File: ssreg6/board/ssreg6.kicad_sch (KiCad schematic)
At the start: 74 parts, among them J12 PROG, U1 YS-12V450A, U2 LTV-354T, U3 ESP32-C3-WROOM-02, U3 FR8205, U5 LM358, U6 LM358, U7 LM358, X1 MAINS, X2 TARIFF

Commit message: WIP
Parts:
- removed H1 (x4): MountingHole, MountingHole:MountingHole_3.7mm_Pad_Via, symbol Mechanical:MountingHole
- removed U1: YS-12V450A, Drake:YS-12V450A, symbol Drake:PSU
- added J2: Display, Connector_PinHeader_2.54mm:PinHeader_1x03_P2.54mm_Vertical, symbol Connector_Generic:Conn_01x03
- added R10, R5, R6, R7, R8, R9: 100k, Resistor_SMD:R_0805_2012Metric_Pad1.20x1.40mm_HandSolder, symbol Device:R
- C10: renamed from C13; footprint Capacitor_SMD:C_0805_2012Metric -> Capacitor_SMD:C_0805_2012Metric_Pad1.18x1.45mm_HandSolder
- C11: renamed from C14; footprint Capacitor_SMD:C_0805_2012Metric -> Capacitor_SMD:C_0805_2012Metric_Pad1.18x1.45mm_HandSolder
- C12: renamed from C15; footprint Capacitor_SMD:C_0805_2012Metric -> Capacitor_SMD:C_0805_2012Metric_Pad1.18x1.45mm_HandSolder
- C13: renamed from C16; footprint Capacitor_SMD:C_0805_2012Metric -> Capacitor_SMD:C_0805_2012Metric_Pad1.18x1.45mm_HandSolder
- C14: renamed from C10; footprint Capacitor_SMD:C_0805_2012Metric -> Capacitor_SMD:C_0805_2012Metric_Pad1.18x1.45mm_HandSolder
- C15: renamed from C17; footprint Capacitor_SMD:C_0805_2012Metric -> Capacitor_SMD:C_0805_2012Metric_Pad1.18x1.45mm_HandSolder
- C16: renamed from C18; footprint Capacitor_SMD:C_0805_2012Metric -> Capacitor_SMD:C_0805_2012Metric_Pad1.18x1.45mm_HandSolder
- C17: renamed from C19; footprint Capacitor_SMD:C_0805_2012Metric -> Capacitor_SMD:C_0805_2012Metric_Pad1.18x1.45mm_HandSolder
- C18: renamed from C20; footprint Capacitor_SMD:C_0805_2012Metric -> Capacitor_SMD:C_0805_2012Metric_Pad1.18x1.45mm_HandSolder
- C19: renamed from C21; footprint Capacitor_SMD:C_0805_2012Metric -> Capacitor_SMD:C_0805_2012Metric_Pad1.18x1.45mm_HandSolder
- C20: renamed from C22; footprint Capacitor_SMD:C_0805_2012Metric -> Capacitor_SMD:C_0805_2012Metric_Pad1.18x1.45mm_HandSolder
- C22: renamed from C6; footprint Capacitor_SMD:C_0805_2012Metric -> Capacitor_SMD:C_0805_2012Metric_Pad1.18x1.45mm_HandSolder
- C6: renamed from C8; footprint Capacitor_SMD:C_0805_2012Metric -> Capacitor_SMD:C_0805_2012Metric_Pad1.18x1.45mm_HandSolder
- C7: footprint Capacitor_SMD:C_0805_2012Metric -> Capacitor_SMD:C_0805_2012Metric_Pad1.18x1.45mm_HandSolder
- C7: renamed from C9; footprint Capacitor_SMD:C_0805_2012Metric -> Capacitor_SMD:C_0805_2012Metric_Pad1.18x1.45mm_HandSolder
- C8: renamed from C11; footprint Capacitor_SMD:C_0805_2012Metric -> Capacitor_SMD:C_0805_2012Metric_Pad1.18x1.45mm_HandSolder
- C9: renamed from C12; footprint Capacitor_SMD:C_0805_2012Metric -> Capacitor_SMD:C_0805_2012Metric_Pad1.18x1.45mm_HandSolder
- D1: footprint LED_SMD:LED_0805_2012Metric -> LED_SMD:LED_0805_2012Metric_Pad1.15x1.40mm_HandSolder
- R11: renamed from R5; footprint Resistor_SMD:R_0805_2012Metric -> Resistor_SMD:R_0805_2012Metric_Pad1.20x1.40mm_HandSolder
- R12: renamed from R6; footprint Resistor_SMD:R_0805_2012Metric -> Resistor_SMD:R_0805_2012Metric_Pad1.20x1.40mm_HandSolder
- R13: renamed from R7; footprint Resistor_SMD:R_0805_2012Metric -> Resistor_SMD:R_0805_2012Metric_Pad1.20x1.40mm_HandSolder
- R14: renamed from R8; footprint Resistor_SMD:R_0805_2012Metric -> Resistor_SMD:R_0805_2012Metric_Pad1.20x1.40mm_HandSolder
- R15: renamed from R9; footprint Resistor_SMD:R_0805_2012Metric -> Resistor_SMD:R_0805_2012Metric_Pad1.20x1.40mm_HandSolder
- R16: renamed from R10; footprint Resistor_SMD:R_0805_2012Metric -> Resistor_SMD:R_0805_2012Metric_Pad1.20x1.40mm_HandSolder
- R17: renamed from R11; footprint Resistor_SMD:R_0805_2012Metric -> Resistor_SMD:R_0805_2012Metric_Pad1.20x1.40mm_HandSolder
- R18: renamed from R12; footprint Resistor_SMD:R_0805_2012Metric -> Resistor_SMD:R_0805_2012Metric_Pad1.20x1.40mm_HandSolder
- R19: renamed from R13; footprint Resistor_SMD:R_0805_2012Metric -> Resistor_SMD:R_0805_2012Metric_Pad1.20x1.40mm_HandSolder
- R20: renamed from R14; footprint Resistor_SMD:R_0805_2012Metric -> Resistor_SMD:R_0805_2012Metric_Pad1.20x1.40mm_HandSolder
- R21: renamed from R15; footprint Resistor_SMD:R_0805_2012Metric -> Resistor_SMD:R_0805_2012Metric_Pad1.20x1.40mm_HandSolder
- R22: renamed from R16; footprint Resistor_SMD:R_0805_2012Metric -> Resistor_SMD:R_0805_2012Metric_Pad1.20x1.40mm_HandSolder
- R23: renamed from R17; footprint Resistor_SMD:R_0805_2012Metric -> Resistor_SMD:R_0805_2012Metric_Pad1.20x1.40mm_HandSolder
- R24: renamed from R18; footprint Resistor_SMD:R_0805_2012Metric -> Resistor_SMD:R_0805_2012Metric_Pad1.20x1.40mm_HandSolder
- R25: renamed from R19; footprint Resistor_SMD:R_0805_2012Metric -> Resistor_SMD:R_0805_2012Metric_Pad1.20x1.40mm_HandSolder
- R26: renamed from R20; footprint Resistor_SMD:R_0805_2012Metric -> Resistor_SMD:R_0805_2012Metric_Pad1.20x1.40mm_HandSolder
- R27: renamed from R21; footprint Resistor_SMD:R_0805_2012Metric -> Resistor_SMD:R_0805_2012Metric_Pad1.20x1.40mm_HandSolder
- R28: renamed from R22; footprint Resistor_SMD:R_0805_2012Metric -> Resistor_SMD:R_0805_2012Metric_Pad1.20x1.40mm_HandSolder
- R29: renamed from R23; footprint Resistor_SMD:R_0805_2012Metric -> Resistor_SMD:R_0805_2012Metric_Pad1.20x1.40mm_HandSolder
- R30: renamed from R24; footprint Resistor_SMD:R_0805_2012Metric -> Resistor_SMD:R_0805_2012Metric_Pad1.20x1.40mm_HandSolder
- R31: renamed from R25; footprint Resistor_SMD:R_0805_2012Metric -> Resistor_SMD:R_0805_2012Metric_Pad1.20x1.40mm_HandSolder
- R32: renamed from R26; footprint Resistor_SMD:R_0805_2012Metric -> Resistor_SMD:R_0805_2012Metric_Pad1.20x1.40mm_HandSolder
- R33: renamed from R27; footprint Resistor_SMD:R_0805_2012Metric -> Resistor_SMD:R_0805_2012Metric_Pad1.20x1.40mm_HandSolder
- R34: renamed from R28; footprint Resistor_SMD:R_0805_2012Metric -> Resistor_SMD:R_0805_2012Metric_Pad1.20x1.40mm_HandSolder
- R36: renamed from R29; footprint Resistor_SMD:R_0805_2012Metric -> Resistor_SMD:R_0805_2012Metric_Pad1.20x1.40mm_HandSolder
- R37: renamed from R30; footprint Resistor_SMD:R_0805_2012Metric -> Resistor_SMD:R_0805_2012Metric_Pad1.20x1.40mm_HandSolder
- R38: renamed from R31; footprint Resistor_SMD:R_0805_2012Metric -> Resistor_SMD:R_0805_2012Metric_Pad1.20x1.40mm_HandSolder
- R39: renamed from R3; footprint Resistor_SMD:R_0805_2012Metric -> Resistor_SMD:R_0805_2012Metric_Pad1.20x1.40mm_HandSolder
- R40: renamed from R4; footprint Resistor_SMD:R_0805_2012Metric -> Resistor_SMD:R_0805_2012Metric_Pad1.20x1.40mm_HandSolder
- R5: footprint Resistor_SMD:R_0805_2012Metric -> Resistor_SMD:R_0805_2012Metric_Pad1.20x1.40mm_HandSolder
- X1: value MAINS -> 12V
- renumbered C4 to C21, R2 to R35, U5 to U4, U6 to U5, U7 to U6, U2 to U7
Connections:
- net +12V: now also X1.2 (Pin_2)
- net +3V3: now also J2.3 (Pin_3)
- net DOUT0: now also R5.2
- net DOUT1: now also R6.2
- net DOUT2: now also R7.2
- net DOUT3: now also R8.2
- net DOUT4: now also R9.2
- net DOUT5: now also R10.2
- net GND: now also X1.1 (Pin_1), J2.1 (Pin_1), R10.1, R5.1, R6.1, R7.1, R8.1, R9.1
- net DISP: now reaches U3.12 (GPIO21/U0TXD)
- net DISP: now also J2.2 (Pin_2)
- no-connect marks 5 -> 4
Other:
- note added: "https://tinyurl.com/26gsxq4a"
- note removed: "https://tinyurl.com/2b23mtv8"
- moved on the sheet: X1

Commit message: library update
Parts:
- U3: footprint Drake:ESP32-C3-WROOM-02 Handsolder -> PCM_Espressif:ESP32-C3-WROOM-02
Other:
- moved on the sheet: C7, J12, J2, R5, X1

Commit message: library update
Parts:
- U3: footprint PCM_Espressif:ESP32-C3-WROOM-02 -> Drake:ESP32-C3-WROOM-02-Handsolder
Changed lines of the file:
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@@
 			)
 		)
-		(property "Footprint" "PCM_Espressif:ESP32-C3-WROOM-02"
+		(property "Footprint" "Drake:ESP32-C3-WROOM-02-Handsolder"
 			(at 68.58 97.79 0)
 			(effects

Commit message: board WIP
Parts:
- J2: value Display -> AUX; footprint Connector_PinHeader_2.54mm:PinHeader_1x03_P2.54mm_Vertical -> Connector_PinHeader_2.54mm:PinHeader_1x05_P2.54mm_Vertical; symbol Connector_Generic:Conn_01x03 -> Connector_Generic:Conn_01x05; now not fitted
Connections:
- net +3V3: now also J2.5 (Pin_5); no longer J2.3 (Pin_3)
- net AUX0: now reaches U3.11 (GPIO20/U0RXD)
- net AUX0: now also J2.2 (Pin_2)
- net AUX2: now reaches U3.8 (GPIO9)
- net AUX2: now also J2.4 (Pin_4)
- net DISP renamed AUX1
- net AUX1: now also J2.3 (Pin_3); no longer J2.2 (Pin_2)
- no-connect marks 4 -> 2
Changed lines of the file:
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@@
 	)
 	(no_connect
-		(at 96.52 46.99)
-	)
-	(no_connect
 		(at 256.54 31.75)
 	)
 	(no_connect
-		(at 96.52 80.01)
-	)
-	(no_connect
 		(at 256.54 29.21)
 	)
@@
 	(wire
 		(pts
-			(xy 87.63 121.92) (xy 92.71 121.92)
+			(xy 87.63 116.84) (xy 92.71 116.84)
 		)
 		(stroke
@@
 		)
 	)
-	(label "DOUT3"
-		(at 139.7 92.71 180)
+	(label "AUX1"
+		(at 96.52 49.53 0)
 		(fields_autoplaced yes)
 		(effects
@@
 				(size 1.27 1.27)
 			)
-			(justify right bottom)
+			(justify left bottom)
 		)
 	)
-	(label "DISP"
-		(at 87.63 124.46 0)
+	(label "DOUT3"
+		(at 139.7 92.71 180)
 		(fields_autoplaced yes)
 		(effects
@@
 				(size 1.27 1.27)
 			)
-			(justify left bottom)
+			(justify right bottom)
 		)
 	)
@@
 		)
 	)
+	(label "AUX1"
+		(at 87.63 121.92 0)
+		(fields_autoplaced yes)
+		(effects
+			(font
+				(size 1.27 1.27)
+			)
+			(justify left bottom)
+		)
+	)
 	(label "LED"
 		(at 241.3 99.06 180)
@@
 		)
 	)
+	(label "AUX0"
+		(at 87.63 124.46 0)
+		(fields_autoplaced yes)
+		(effects
+			(font
+				(size 1.27 1.27)
+			)
+			(justify left bottom)
+		)
+	)
 	(label "DOUT1"
 		(at 139.7 49.53 180)
@@
 		)
 	)
-	(label "DISP"
-		(at 96.52 49.53 0)
+	(label "LED"
+		(at 96.52 72.39 0)
 		(fields_autoplaced yes)
 		(effects
@@
 		)
 	)
-	(label "LED"
-		(at 96.52 72.39 0)
+	(label "AOUT5"
+		(at 195.58 138.43 0)
 		(fields_autoplaced yes)
 		(effects
@@
 		)
 	)
-	(label "AOUT5"
-		(at 195.58 138.43 0)
+	(label "AUX2"
+		(at 96.52 80.01 0)
+		(fields_autoplaced yes)
+		(effects
+			(font
+				(size 1.27 1.27)
+			)
+			(justify left bottom)
+		)
+	)
+	(label "AUX0"
+		(at 96.52 46.99 0)
 		(fields_autoplaced yes)
 		(effects
@@
 		)
 	)
+	(label "AUX2"
+		(at 87.63 119.38 0)
+		(fields_autoplaced yes)
+		(effects
+			(font
+				(size 1.27 1.27)
+			)
+			(justify left bottom)
+		)
+	)
 	(label "DOUT0"
 		(at 139.7 27.94 180)
@@
 	)
 	(symbol
-		(lib_id "Connector_Generic:Conn_01x03")
-		(at 82.55 124.46 180)
+		(lib_id "Connector_Generic:Conn_01x05")
+		(at 82.55 121.92 180)
 		(unit 1)
 		(exclude_from_sim no)
 		(in_bom yes)
 		(on_board yes)
-		(dnp no)
+		(dnp yes)
 		(fields_autoplaced yes)
 		(property "Reference" "J2"
-			(at 82.55 116.5057 0)
+			(at 82.55 110.49 0)
 			(effects
 				(font
@@
 			)
 		)
-		(property "Value" "Display"
-			(at 82.55 118.9299 0)
+		(property "Value" "AUX"
+			(at 82.55 113.03 0)
 			(effects
 				(font
@@
 			)
 		)
-		(property "Footprint" "Connector_PinHeader_2.54mm:PinHeader_1x03_P2.54mm_Vertical"
-			(at 82.55 124.46 0)
+		(property "Footprint" "Connector_PinHeader_2.54mm:PinHeader_1x05_P2.54mm_Vertical"
+			(at 82.55 121.92 0)
 			(effects
 				(font
@@
 		)
 		(property "Datasheet" "~"
-			(at 82.55 124.46 0)
+			(at 82.55 121.92 0)
 			(effects
 				(font
@@
 			)
 		)
-		(property "Description" "Generic connector, single row, 01x03, script generated (kicad-library-utils/schlib/autogen/connector/)"
-			(at 82.55 124.46 0)
+		(property "Description" "Generic connector, single row, 01x05, script generated (kicad-library-utils/schlib/autogen/connector/)"
+			(at 82.55 121.92 0)
 			(effects
 				(font
@@
 		(pin "3"
 		)
+		(pin "4"
+		)
+		(pin "5"
+		)
 		(instances
 			(project "ssreg6"
@@
 	(symbol
 		(lib_id "power:+3.3V")
-		(at 92.71 121.92 270)
+		(at 92.71 116.84 270)
 		(unit 1)
 		(exclude_from_sim no)
@@
 		(dnp no)
 		(property "Reference" "#PWR018"
-			(at 88.9 121.92 0)
+			(at 88.9 116.84 0)
 			(effects
 				(font
@@
 		)
 		(property "Value" "+3V3"
-			(at 97.79 121.92 90)
+			(at 97.79 116.84 90)
 			(effects
 				(font
@@
 		)
 		(property "Footprint" ""
-			(at 92.71 121.92 0)
+			(at 92.71 116.84 0)
 			(effects
 				(font
@@
 		)
 		(property "Datasheet" ""
-			(at 92.71 121.92 0)
+			(at 92.71 116.84 0)
 			(effects
 				(font
@@
 		)
 		(property "Description" "Power symbol creates a global label with name \"+3.3V\""
-			(at 92.71 121.92 0)
+			(at 92.71 116.84 0)
 			(effects
 				(font

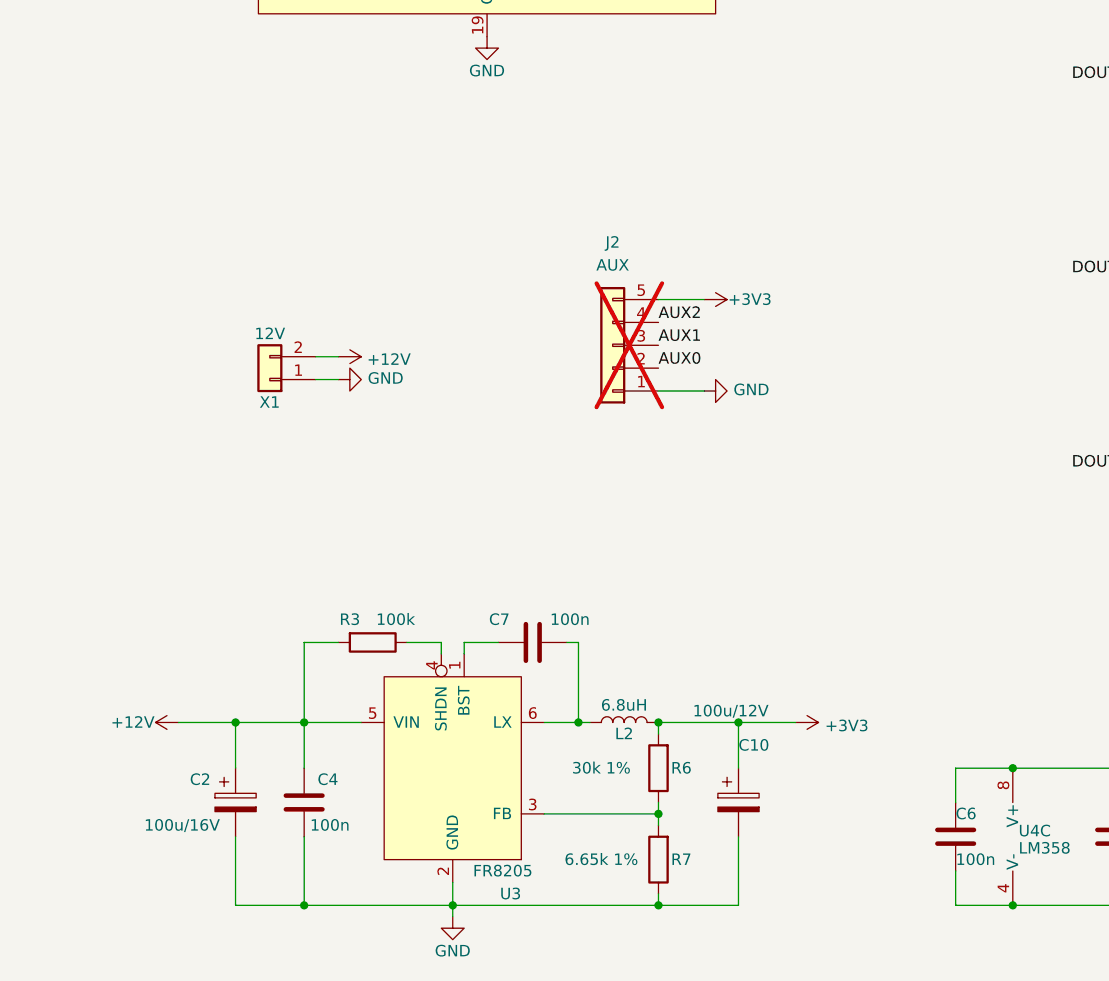
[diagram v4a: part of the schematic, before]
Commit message: ceramic capacitors on PSU & JLC order
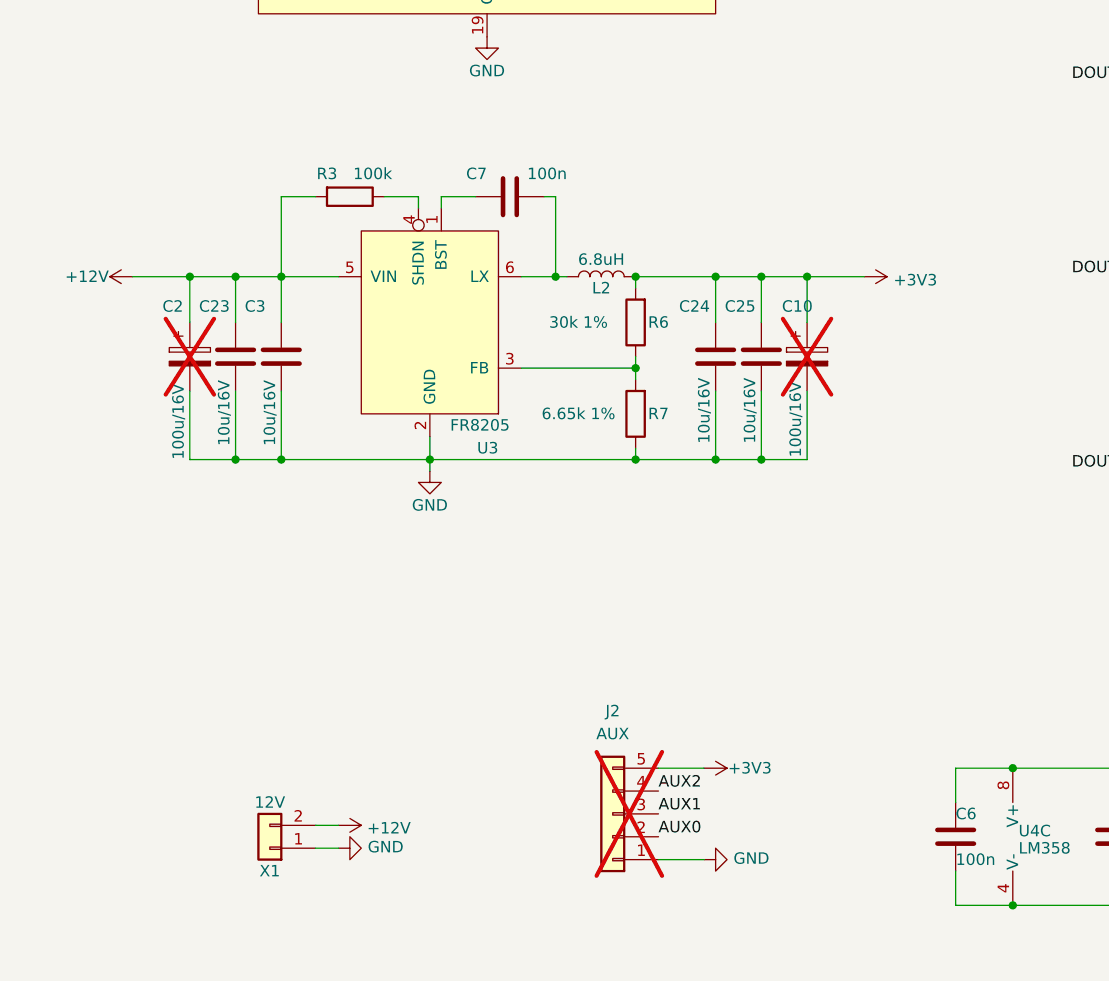
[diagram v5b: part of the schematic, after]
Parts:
- removed C4: 100n, Capacitor_SMD:C_0805_2012Metric_Pad1.18x1.45mm_HandSolder, symbol Device:C
- added C23, C24, C25, C3: 10u/16V, Capacitor_SMD:C_0805_2012Metric_Pad1.18x1.45mm_HandSolder, symbol Device:C
- C10: value 100u/12V -> 100u/16V; now not fitted
- C2: now not fitted
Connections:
- net +12V: now also C23.1, C3.1
- net +3V3: now also C24.1, C25.1
- net GND: now also C23.2, C24.2, C25.2, C3.2
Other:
- moved on the sheet: C7, J2, L2, R3, R6, R7, U3, X1
